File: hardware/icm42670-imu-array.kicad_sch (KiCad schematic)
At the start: 63 parts, among them J1 TC2030-NL, J2 USB_B_Micro, J3 Conn_02x10_Odd_Even, SW1 PTS810, U1 ICM-42670-P, U10 MCP73812T-420I-OT, U2 ICM-42670-P, U3 ICM-42670-P, U4 ICM-42670-P, U5 ICM-42670-P, U6 ICM-42670-P, U7 ICM-42670-P, U8 ICM-42670-P, U9 MDBT50Q-P1MV2

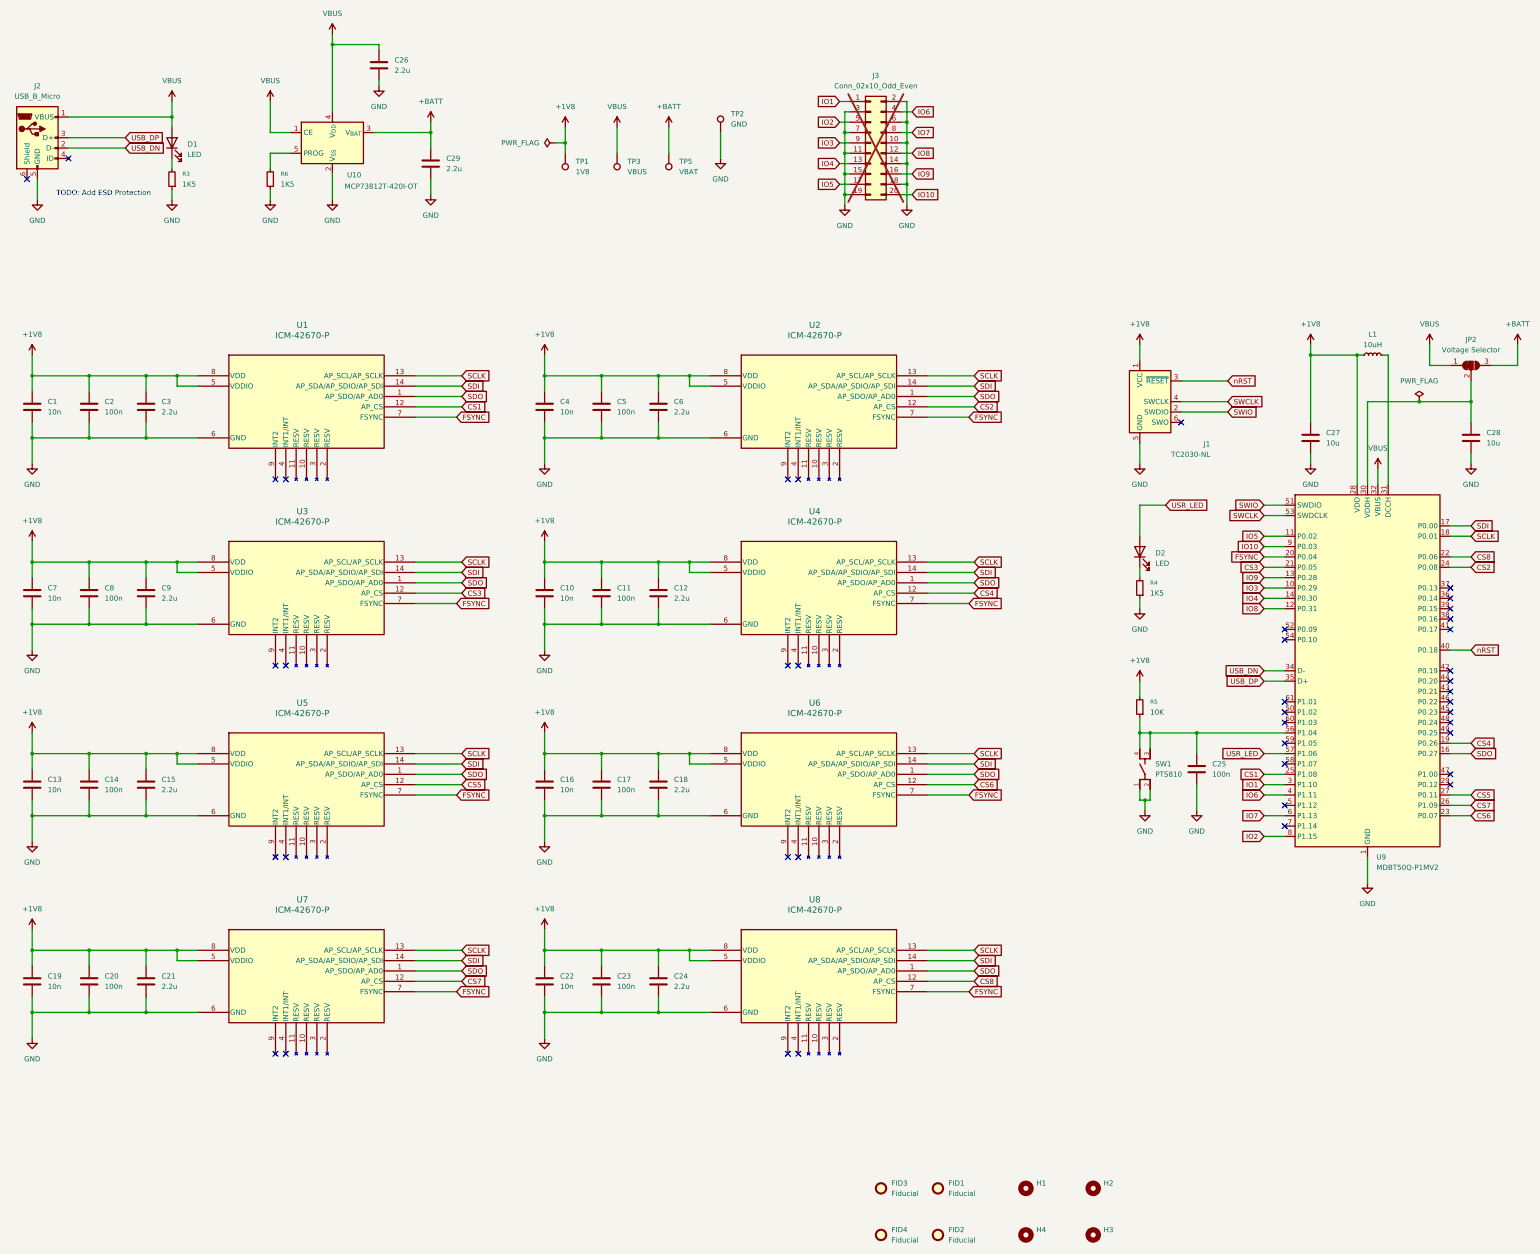
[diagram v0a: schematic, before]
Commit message: feat: add round tracks
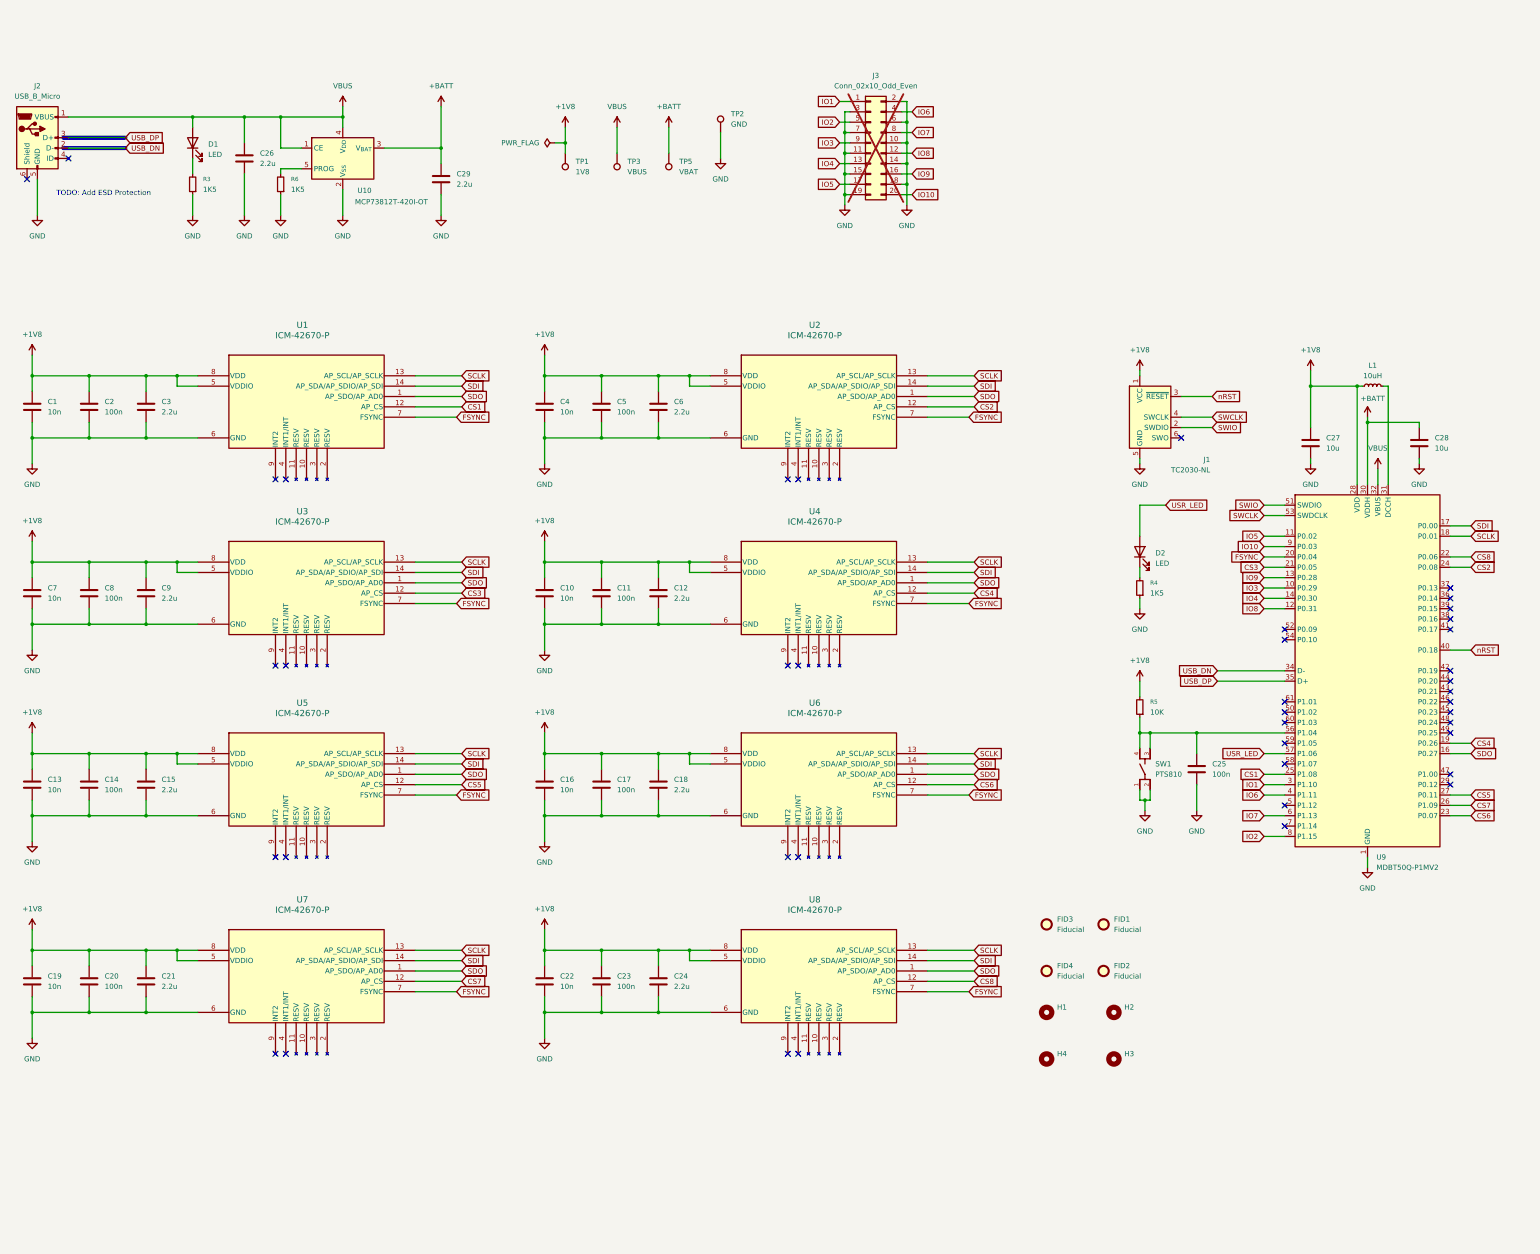
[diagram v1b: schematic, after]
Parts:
- removed JP2: Voltage Selector, Jumper:SolderJumper-3_P1.3mm_Bridged12_RoundedPad1.0x1.5mm, symbol Jumper:SolderJumper_3_Bridged12
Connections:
- net +BATT: now also C28.1, U9.30 (VDDH)
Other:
- moved on the sheet: C26, C27, C28, C29, D1, FID1, FID2, FID3, FID4, H1, H2, H3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
